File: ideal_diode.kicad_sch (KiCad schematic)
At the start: 5 parts, among them Q11 BSC059N04LS6, U18 LM74700

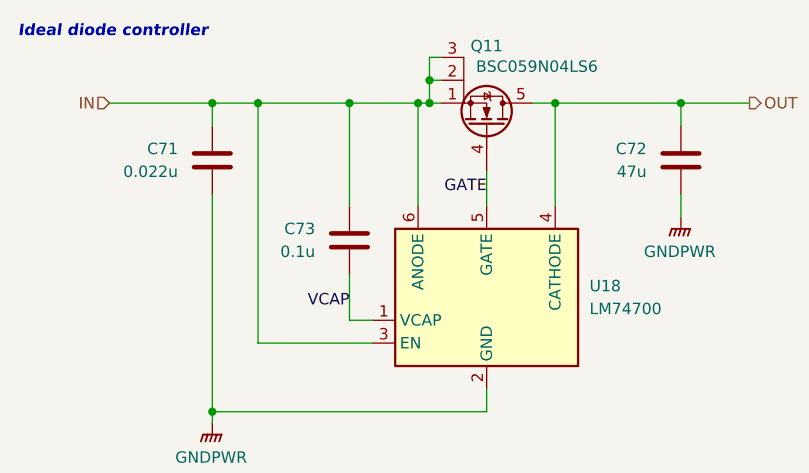
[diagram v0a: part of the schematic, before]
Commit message: Renumbering components
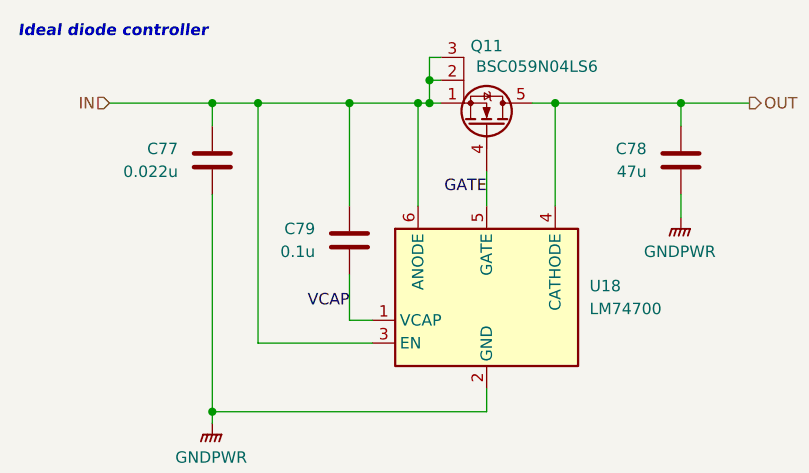
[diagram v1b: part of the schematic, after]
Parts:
- renumbered C71 to C77, C72 to C78, C73 to C79
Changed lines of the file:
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@@
 		(on_board yes)
 		(dnp no)
-		(property "Reference" "C72"
+		(property "Reference" "C78"
 			(at 121.92 36.8299 0)
 			(effects
@@
 			(project "Ideal Diode Rev1"
 				(path "/6197145b-e7d4-44cc-9d90-537b6501bf60/130ec867-c4fa-4318-bea9-b8fc517d0b0a"
-					(reference "C72")
+					(reference "C78")
 					(unit 1)
 				)
@@
 		(on_board yes)
 		(dnp no)
-		(property "Reference" "C71"
+		(property "Reference" "C77"
 			(at 69.85 36.8299 0)
 			(effects
@@
 			(project "Ideal Diode Rev1"
 				(path "/6197145b-e7d4-44cc-9d90-537b6501bf60/130ec867-c4fa-4318-bea9-b8fc517d0b0a"
-					(reference "C71")
+					(reference "C77")
 					(unit 1)
 				)
@@
 		(dnp no)
 		(fields_autoplaced yes)
-		(property "Reference" "#PWR0105"
+		(property "Reference" "#PWR0104"
 			(at 73.66 72.39 0)
 			(effects
@@
 			(project "Ideal Diode Rev1"
 				(path "/6197145b-e7d4-44cc-9d90-537b6501bf60/130ec867-c4fa-4318-bea9-b8fc517d0b0a"
-					(reference "#PWR0105")
+					(reference "#PWR0104")
 					(unit 1)
 				)
@@
 		(on_board yes)
 		(dnp no)
-		(property "Reference" "C73"
+		(property "Reference" "C79"
 			(at 85.09 45.7199 0)
 			(effects
@@
 			(project "Ideal Diode Rev1"
 				(path "/6197145b-e7d4-44cc-9d90-537b6501bf60/130ec867-c4fa-4318-bea9-b8fc517d0b0a"
-					(reference "C73")
+					(reference "C79")
 					(unit 1)
 				)
@@
 		(dnp no)
 		(fields_autoplaced yes)
-		(property "Reference" "#PWR0104"
+		(property "Reference" "#PWR0103"
 			(at 125.73 49.53 0)
 			(effects
@@
 			(project "Ideal Diode Rev1"
 				(path "/6197145b-e7d4-44cc-9d90-537b6501bf60/130ec867-c4fa-4318-bea9-b8fc517d0b0a"
-					(reference "#PWR0104")
-					(unit 1)
-				)
+					(reference "#PWR0103")
+					(unit 1)
+				)

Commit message: Sourcing various parts
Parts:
- U18: Mouser Part Number (none) -> 595-LM74700QDBVRQ1
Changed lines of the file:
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@@
+			)
+		)
+		(property "Mouser Part Number" "595-LM74700QDBVRQ1"
+			(at 104.14 53.34 0)
+			(effects
+				(font
+					(size 1.27 1.27)
+				)
+				(hide yes)
 			)
 		)

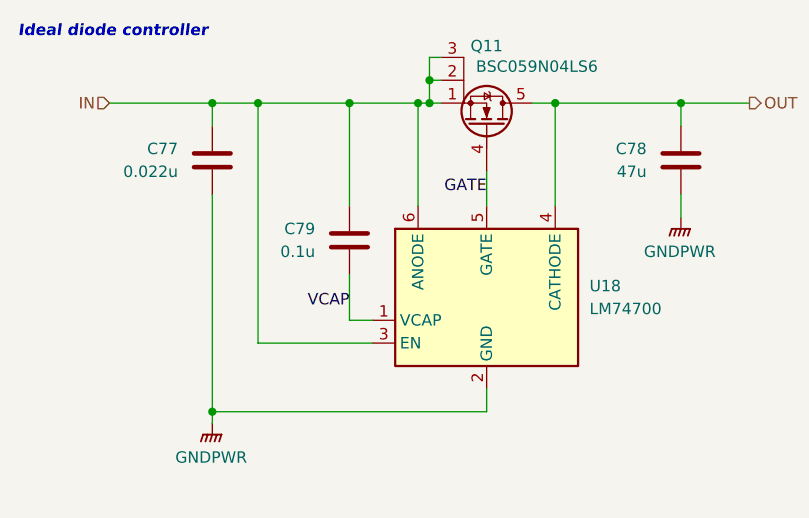
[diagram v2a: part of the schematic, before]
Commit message: Specc'd all components + started creating rev 1b boards
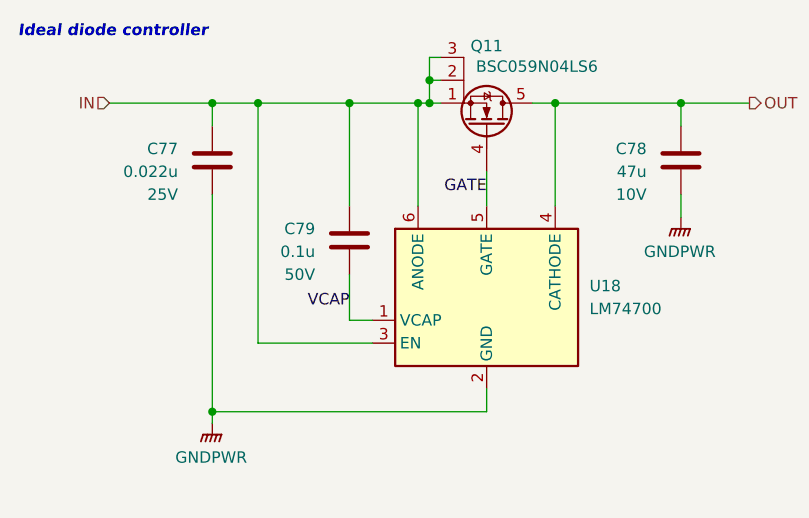
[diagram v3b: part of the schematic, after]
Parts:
- C77: Mouser Part Number (none) -> 710-885012206067; Voltage Rating (none) -> 25V
- C78: footprint Capacitor_SMD:C_0603_1608Metric_Pad1.08x0.95mm_HandSolder -> Capacitor_SMD:C_1206_3216Metric_Pad1.33x1.80mm_HandSolder; Mouser Part Number (none) -> 81-GRM31CR61A476ME5K; Voltage Rating (none) -> 10V
- C79: Mouser Part Number (none) -> 581-KGM15BR71H104JT; Voltage Rating (none) -> 50V
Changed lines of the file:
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@@
 			)
 		)
-		(property "Footprint" "Capacitor_SMD:C_0603_1608Metric_Pad1.08x0.95mm_HandSolder"
+		(property "Footprint" "Capacitor_SMD:C_1206_3216Metric_Pad1.33x1.80mm_HandSolder"
 			(at 124.7648 41.91 0)
 			(effects
@@
 					(size 1.27 1.27)
 				)
+			)
+		)
+		(property "Mouser Part Number" "81-GRM31CR61A476ME5K"
+			(at 125.73 38.1 0)
+			(effects
+				(font
+					(size 1.27 1.27)
+				)
+				(hide yes)
+			)
+		)
+		(property "Voltage Rating" "10V"
+			(at 121.92 41.91 0)
+			(effects
+				(font
+					(size 1.27 1.27)
+				)
+				(justify left)
 			)
 		)
@@
 			)
 		)
+		(property "Mouser Part Number" "710-885012206067"
+			(at 73.66 38.1 0)
+			(effects
+				(font
+					(size 1.27 1.27)
+				)
+				(hide yes)
+			)
+		)
+		(property "Voltage Rating" "25V"
+			(at 69.85 41.91 0)
+			(effects
+				(font
+					(size 1.27 1.27)
+				)
+				(justify left)
+			)
+		)
 		(pin "1"
 		)
@@
 			)
 		)
-		(property "Datasheet" "~"
+		(property "Datasheet" "https://www.mouser.com/datasheet/2/40/KGM_X7R-3223212.pdf"
 			(at 88.9 46.99 0)
 			(effects
@@
 			)
 		)
+		(property "Mouser Part Number" "581-KGM15BR71H104JT"
+			(at 88.9 46.99 0)
+			(effects
+				(font
+					(size 1.27 1.27)
+				)
+				(hide yes)
+			)
+		)
+		(property "Voltage Rating" "50V"
+			(at 85.09 50.8 0)
+			(effects
+				(font
+					(size 1.27 1.27)
+				)
+				(justify left)
+			)
+		)

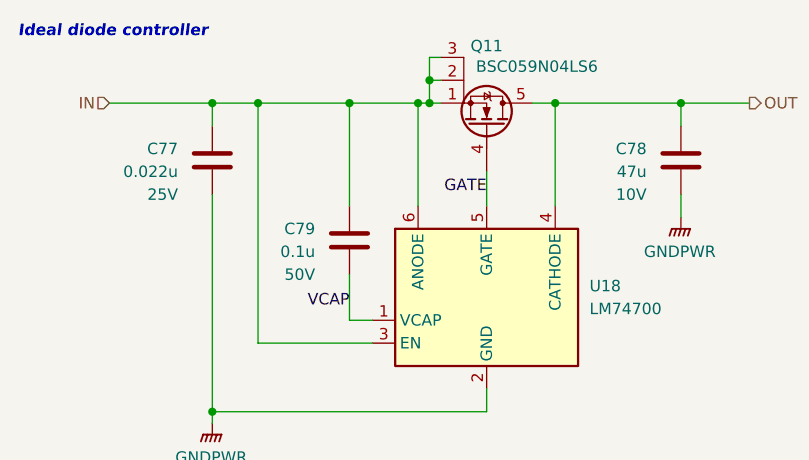
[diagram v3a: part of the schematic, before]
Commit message: Add test points to all subsheets
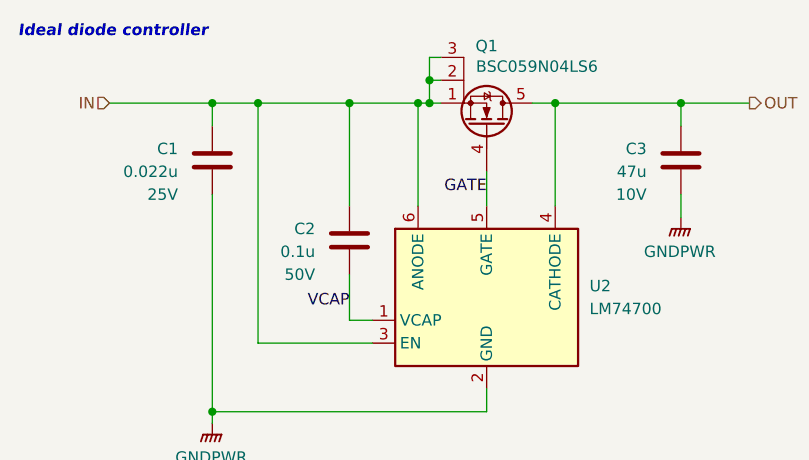
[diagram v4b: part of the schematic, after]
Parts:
- renumbered C77 to C1, C79 to C2, C78 to C3, Q11 to Q1, U18 to U2
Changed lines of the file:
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@@
 		(on_board yes)
 		(dnp no)
-		(property "Reference" "C78"
+		(property "Reference" "C?"
 			(at 121.92 36.8299 0)
 			(effects
@@
 				(path "/6197145b-e7d4-44cc-9d90-537b6501bf60/130ec867-c4fa-4318-bea9-b8fc517d0b0a"
 					(reference "C78")
+					(unit 1)
+				)
+			)
+			(project "Rev 1B"
+				(path "/e5f99deb-ef42-4c5f-b80a-388477910e20/7bf219df-2692-4f86-9971-baba03c19447"
+					(reference "C?")
 					(unit 1)
 				)
@@
 		(on_board yes)
 		(dnp no)
-		(property "Reference" "C77"
+		(property "Reference" "C?"
 			(at 69.85 36.8299 0)
 			(effects
@@
 				(path "/6197145b-e7d4-44cc-9d90-537b6501bf60/130ec867-c4fa-4318-bea9-b8fc517d0b0a"
 					(reference "C77")
+					(unit 1)
+				)
+			)
+			(project "Rev 1B"
+				(path "/e5f99deb-ef42-4c5f-b80a-388477910e20/7bf219df-2692-4f86-9971-baba03c19447"
+					(reference "C?")
 					(unit 1)
 				)
@@
 		(dnp no)
 		(fields_autoplaced yes)
-		(property "Reference" "#PWR0104"
+		(property "Reference" "#PWR?"
 			(at 73.66 72.39 0)
 			(effects
@@
 				(path "/6197145b-e7d4-44cc-9d90-537b6501bf60/130ec867-c4fa-4318-bea9-b8fc517d0b0a"
 					(reference "#PWR0104")
+					(unit 1)
+				)
+			)
+			(project "Rev 1B"
+				(path "/e5f99deb-ef42-4c5f-b80a-388477910e20/7bf219df-2692-4f86-9971-baba03c19447"
+					(reference "#PWR?")
 					(unit 1)
 				)
@@
 		(on_board yes)
 		(dnp no)
-		(property "Reference" "C79"
+		(property "Reference" "C?"
 			(at 85.09 45.7199 0)
 			(effects
@@
 				(path "/6197145b-e7d4-44cc-9d90-537b6501bf60/130ec867-c4fa-4318-bea9-b8fc517d0b0a"
 					(reference "C79")
+					(unit 1)
+				)
+			)
+			(project "Rev 1B"
+				(path "/e5f99deb-ef42-4c5f-b80a-388477910e20/7bf219df-2692-4f86-9971-baba03c19447"
+					(reference "C?")
 					(unit 1)
 				)
@@
 		(on_board yes)
 		(dnp no)
-		(property "Reference" "Q11"
+		(property "Reference" "Q?"
 			(at 104.14 25.4 90)
 			(effects
@@
 				(path "/6197145b-e7d4-44cc-9d90-537b6501bf60/130ec867-c4fa-4318-bea9-b8fc517d0b0a"
 					(reference "Q11")
+					(unit 1)
+				)
+			)
+			(project "Rev 1B"
+				(path "/e5f99deb-ef42-4c5f-b80a-388477910e20/7bf219df-2692-4f86-9971-baba03c19447"
+					(reference "Q?")
 					(unit 1)
 				)
@@
 		(dnp no)
 		(fields_autoplaced yes)
-		(property "Reference" "U18"
+		(property "Reference" "U?"
 			(at 115.57 52.0699 0)
 			(effects
@@
 				(path "/6197145b-e7d4-44cc-9d90-537b6501bf60/130ec867-c4fa-4318-bea9-b8fc517d0b0a"
 					(reference "U18")
+					(unit 1)
+				)
+			)
+			(project "Rev 1B"
+				(path "/e5f99deb-ef42-4c5f-b80a-388477910e20/7bf219df-2692-4f86-9971-baba03c19447"
+					(reference "U?")
 					(unit 1)
 				)
@@
 		(dnp no)
 		(fields_autoplaced yes)
-		(property "Reference" "#PWR0103"
+		(property "Reference" "#PWR?"
 			(at 125.73 49.53 0)
 			(effects
@@
 					(unit 1)
 				)
+			)
+			(project "Rev 1B"
+				(path "/e5f99deb-ef42-4c5f-b80a-388477910e20/7bf219df-2692-4f86-9971-baba03c19447"
+					(reference "#PWR?")
+					(unit 1)
+				)

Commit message: Renumbered components for rev 1b layout
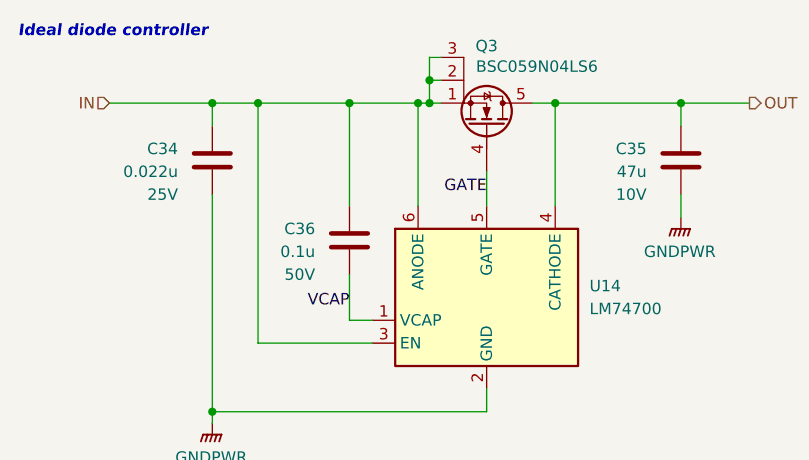
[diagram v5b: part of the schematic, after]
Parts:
- renumbered C1 to C34, C3 to C35, C2 to C36, Q1 to Q3, U2 to U14
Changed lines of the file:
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@@
 		(on_board yes)
 		(dnp no)
-		(property "Reference" "C?"
+		(property "Reference" "C35"
 			(at 121.92 36.8299 0)
 			(effects
@@
 			(project "Rev 1B"
 				(path "/e5f99deb-ef42-4c5f-b80a-388477910e20/7bf219df-2692-4f86-9971-baba03c19447"
-					(reference "C?")
+					(reference "C35")
 					(unit 1)
 				)
@@
 		(on_board yes)
 		(dnp no)
-		(property "Reference" "C?"
+		(property "Reference" "C34"
 			(at 69.85 36.8299 0)
 			(effects
@@
 			(project "Rev 1B"
 				(path "/e5f99deb-ef42-4c5f-b80a-388477910e20/7bf219df-2692-4f86-9971-baba03c19447"
-					(reference "C?")
+					(reference "C34")
 					(unit 1)
 				)
@@
 		(dnp no)
 		(fields_autoplaced yes)
-		(property "Reference" "#PWR?"
+		(property "Reference" "#PWR095"
 			(at 73.66 72.39 0)
 			(effects
@@
 			(project "Rev 1B"
 				(path "/e5f99deb-ef42-4c5f-b80a-388477910e20/7bf219df-2692-4f86-9971-baba03c19447"
-					(reference "#PWR?")
+					(reference "#PWR095")
 					(unit 1)
 				)
@@
 		(on_board yes)
 		(dnp no)
-		(property "Reference" "C?"
+		(property "Reference" "C36"
 			(at 85.09 45.7199 0)
 			(effects
@@
 			(project "Rev 1B"
 				(path "/e5f99deb-ef42-4c5f-b80a-388477910e20/7bf219df-2692-4f86-9971-baba03c19447"
-					(reference "C?")
+					(reference "C36")
 					(unit 1)
 				)
@@
 		(on_board yes)
 		(dnp no)
-		(property "Reference" "Q?"
+		(property "Reference" "Q3"
 			(at 104.14 25.4 90)
 			(effects
@@
 			(project "Rev 1B"
 				(path "/e5f99deb-ef42-4c5f-b80a-388477910e20/7bf219df-2692-4f86-9971-baba03c19447"
-					(reference "Q?")
+					(reference "Q3")
 					(unit 1)
 				)
@@
 		(dnp no)
 		(fields_autoplaced yes)
-		(property "Reference" "U?"
+		(property "Reference" "U14"
 			(at 115.57 52.0699 0)
 			(effects
@@
 			(project "Rev 1B"
 				(path "/e5f99deb-ef42-4c5f-b80a-388477910e20/7bf219df-2692-4f86-9971-baba03c19447"
-					(reference "U?")
+					(reference "U14")
 					(unit 1)
 				)
@@
 		(dnp no)
 		(fields_autoplaced yes)
-		(property "Reference" "#PWR?"
+		(property "Reference" "#PWR094"
 			(at 125.73 49.53 0)
 			(effects
@@
 			(project "Rev 1B"
 				(path "/e5f99deb-ef42-4c5f-b80a-388477910e20/7bf219df-2692-4f86-9971-baba03c19447"
-					(reference "#PWR?")
-					(unit 1)
-				)
+					(reference "#PWR094")
+					(unit 1)
+				)

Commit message: Update PCB to fix ERC breaks
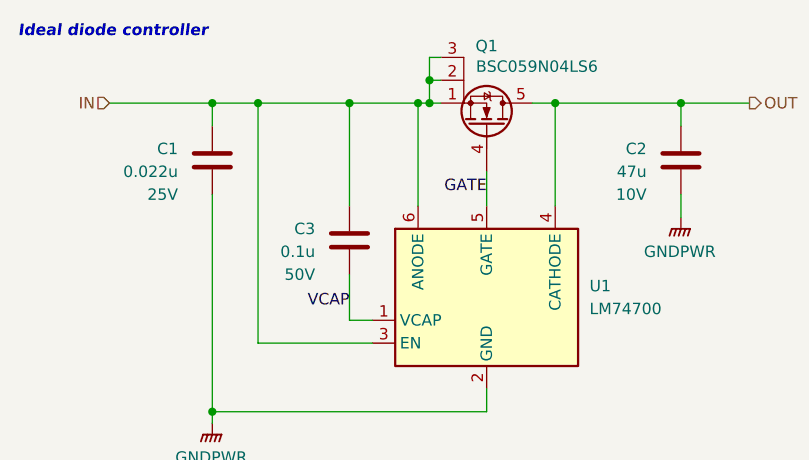
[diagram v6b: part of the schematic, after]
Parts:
- renumbered C34 to C1, C35 to C2, C36 to C3, Q3 to Q1, U14 to U1
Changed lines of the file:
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@@
 		(on_board yes)
 		(dnp no)
-		(property "Reference" "C35"
+		(property "Reference" "C2"
 			(at 121.92 36.8299 0)
 			(effects
@@
 				(path "/6197145b-e7d4-44cc-9d90-537b6501bf60/130ec867-c4fa-4318-bea9-b8fc517d0b0a"
 					(reference "C78")
+					(unit 1)
+				)
+			)
+			(project "Buck1 1B"
+				(path "/80afba09-f71a-481c-a343-2cbd993e7569/435402b6-45a2-41c3-bc2a-be9f3f280d73"
+					(reference "C2")
 					(unit 1)
 				)
@@
 		(on_board yes)
 		(dnp no)
-		(property "Reference" "C34"
+		(property "Reference" "C1"
 			(at 69.85 36.8299 0)
 			(effects
@@
 				(path "/6197145b-e7d4-44cc-9d90-537b6501bf60/130ec867-c4fa-4318-bea9-b8fc517d0b0a"
 					(reference "C77")
+					(unit 1)
+				)
+			)
+			(project "Buck1 1B"
+				(path "/80afba09-f71a-481c-a343-2cbd993e7569/435402b6-45a2-41c3-bc2a-be9f3f280d73"
+					(reference "C1")
 					(unit 1)
 				)
@@
 		(dnp no)
 		(fields_autoplaced yes)
-		(property "Reference" "#PWR095"
+		(property "Reference" "#PWR03"
 			(at 73.66 72.39 0)
 			(effects
@@
 				(path "/6197145b-e7d4-44cc-9d90-537b6501bf60/130ec867-c4fa-4318-bea9-b8fc517d0b0a"
 					(reference "#PWR0104")
+					(unit 1)
+				)
+			)
+			(project "Buck1 1B"
+				(path "/80afba09-f71a-481c-a343-2cbd993e7569/435402b6-45a2-41c3-bc2a-be9f3f280d73"
+					(reference "#PWR03")
 					(unit 1)
 				)
@@
 		(on_board yes)
 		(dnp no)
-		(property "Reference" "C36"
+		(property "Reference" "C3"
 			(at 85.09 45.7199 0)
 			(effects
@@
 				(path "/6197145b-e7d4-44cc-9d90-537b6501bf60/130ec867-c4fa-4318-bea9-b8fc517d0b0a"
 					(reference "C79")
+					(unit 1)
+				)
+			)
+			(project "Buck1 1B"
+				(path "/80afba09-f71a-481c-a343-2cbd993e7569/435402b6-45a2-41c3-bc2a-be9f3f280d73"
+					(reference "C3")
 					(unit 1)
 				)
@@
 		(on_board yes)
 		(dnp no)
-		(property "Reference" "Q3"
+		(property "Reference" "Q1"
 			(at 104.14 25.4 90)
 			(effects
@@
 				(path "/6197145b-e7d4-44cc-9d90-537b6501bf60/130ec867-c4fa-4318-bea9-b8fc517d0b0a"
 					(reference "Q11")
+					(unit 1)
+				)
+			)
+			(project "Buck1 1B"
+				(path "/80afba09-f71a-481c-a343-2cbd993e7569/435402b6-45a2-41c3-bc2a-be9f3f280d73"
+					(reference "Q1")
 					(unit 1)
 				)
@@
 		(dnp no)
 		(fields_autoplaced yes)
-		(property "Reference" "U14"
+		(property "Reference" "U1"
 			(at 115.57 52.0699 0)
 			(effects
@@
 				(path "/6197145b-e7d4-44cc-9d90-537b6501bf60/130ec867-c4fa-4318-bea9-b8fc517d0b0a"
 					(reference "U18")
+					(unit 1)
+				)
+			)
+			(project "Buck1 1B"
+				(path "/80afba09-f71a-481c-a343-2cbd993e7569/435402b6-45a2-41c3-bc2a-be9f3f280d73"
+					(reference "U1")
 					(unit 1)
 				)
@@
 		(dnp no)
 		(fields_autoplaced yes)
-		(property "Reference" "#PWR094"
+		(property "Reference" "#PWR02"
 			(at 125.73 49.53 0)
 			(effects
@@
 					(unit 1)
 				)
+			)
+			(project "Buck1 1B"
+				(path "/80afba09-f71a-481c-a343-2cbd993e7569/435402b6-45a2-41c3-bc2a-be9f3f280d73"
+					(reference "#PWR02")
+					(unit 1)
+				)
